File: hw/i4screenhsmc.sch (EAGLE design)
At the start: 67 parts, among them CON1 IPHONE4_LCD_CONN, J1 QTH-090-XX-X-D-A, Q6 BSS84, U1 TPS622XX, U2 TPS622XX

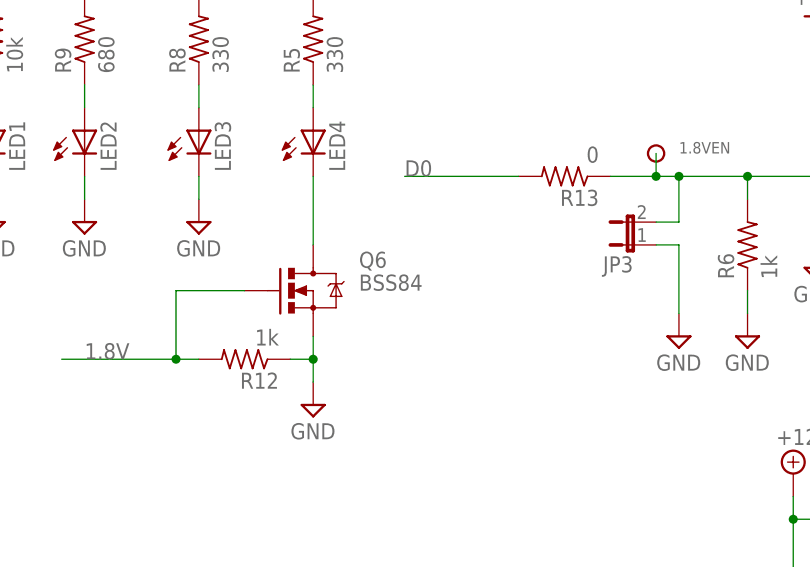
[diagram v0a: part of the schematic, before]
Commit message: the N-channel FET is a BSS138, not a BSS84 (which is P-channel)
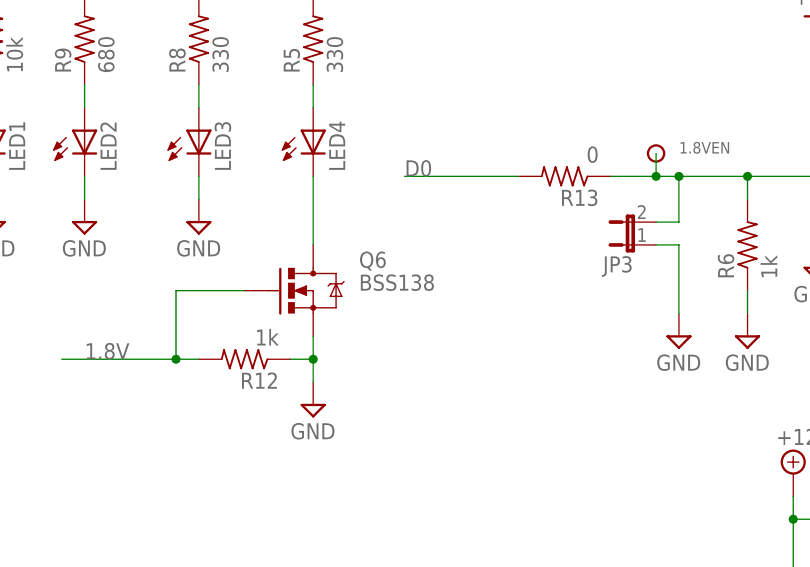
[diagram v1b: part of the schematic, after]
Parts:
- Q6: value BSS84 -> BSS138
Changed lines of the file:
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@@
 <?xml version="1.0" encoding="utf-8"?>
 <!DOCTYPE eagle SYSTEM "eagle.dtd">
-<eagle version="6.5.0">
+<eagle version="6.6.0">
 <drawing>
 <settings>
@@
 <part name="LED3" library="led" deviceset="LED" device="CHIP-LED0805"/>
 <part name="LED4" library="led" deviceset="LED" device="CHIP-LED0805"/>
-<part name="Q6" library="SparkFun" deviceset="MOSFET-NCHANNEL" device="SMD" value="BSS84"/>
+<part name="Q6" library="SparkFun" deviceset="MOSFET-NCHANNEL" device="SMD" value="BSS138"/>
 <part name="R5" library="rcl" deviceset="R-US_" device="R0805" value="330"/>
 <part name="R8" library="rcl" deviceset="R-US_" device="R0805" value="330"/>
